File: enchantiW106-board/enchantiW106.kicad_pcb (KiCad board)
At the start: 2 copper layers, 62.2 x 25.4 mm, 66 parts, among them J1 USB_C_Receptacle_USB2.0, SW1 B3U-1000P, SW2 B3U-1000P, U1 USBLC6-2P6, U11 MAX17262REWL+T, U12 BQ25185DLHR, U13 ICM-42670-P, U2 MMC5633NJL, U3 IRIS-W106-00B, U4 NCP167AMX330TBG, U5 CP2102N-Axx-xQFN20, U9 NCP167AMX330TBG

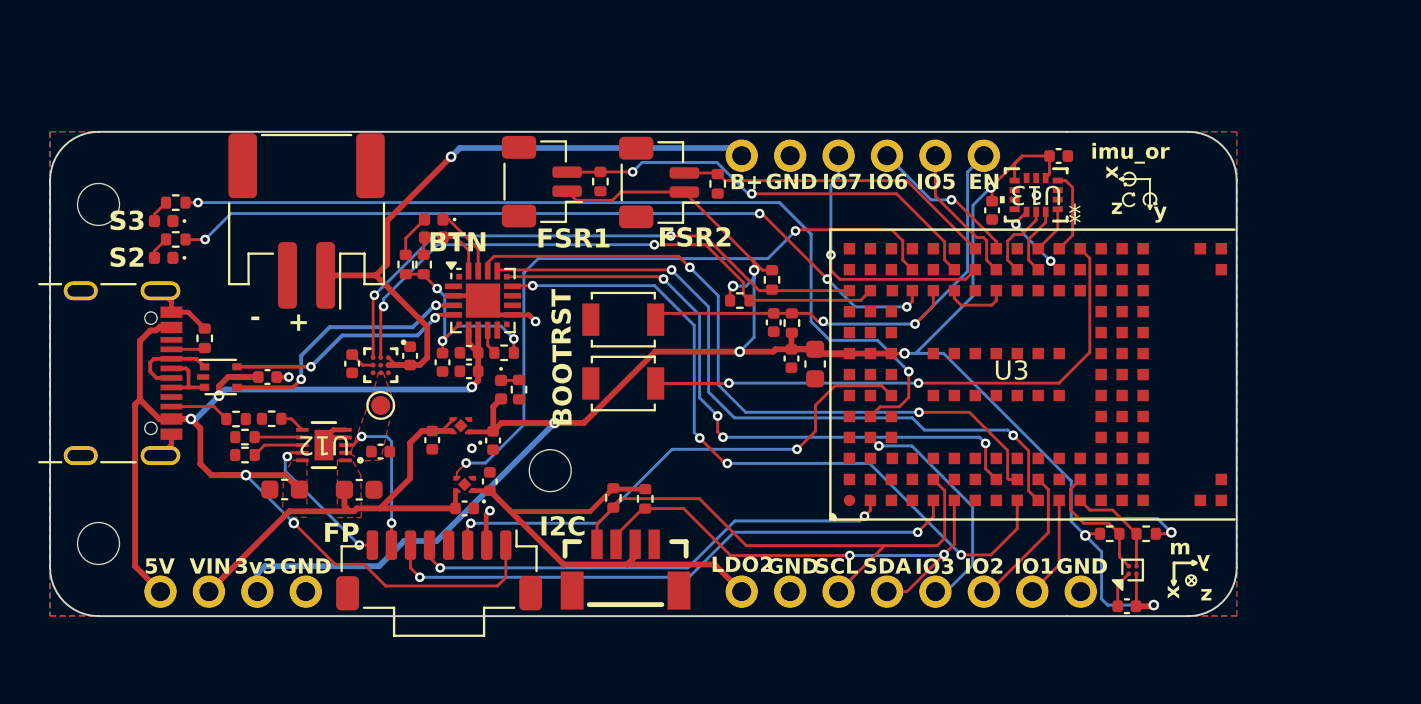
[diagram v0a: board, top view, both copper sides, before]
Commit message: removed all fine pitch components, finished initial board layout and drc check
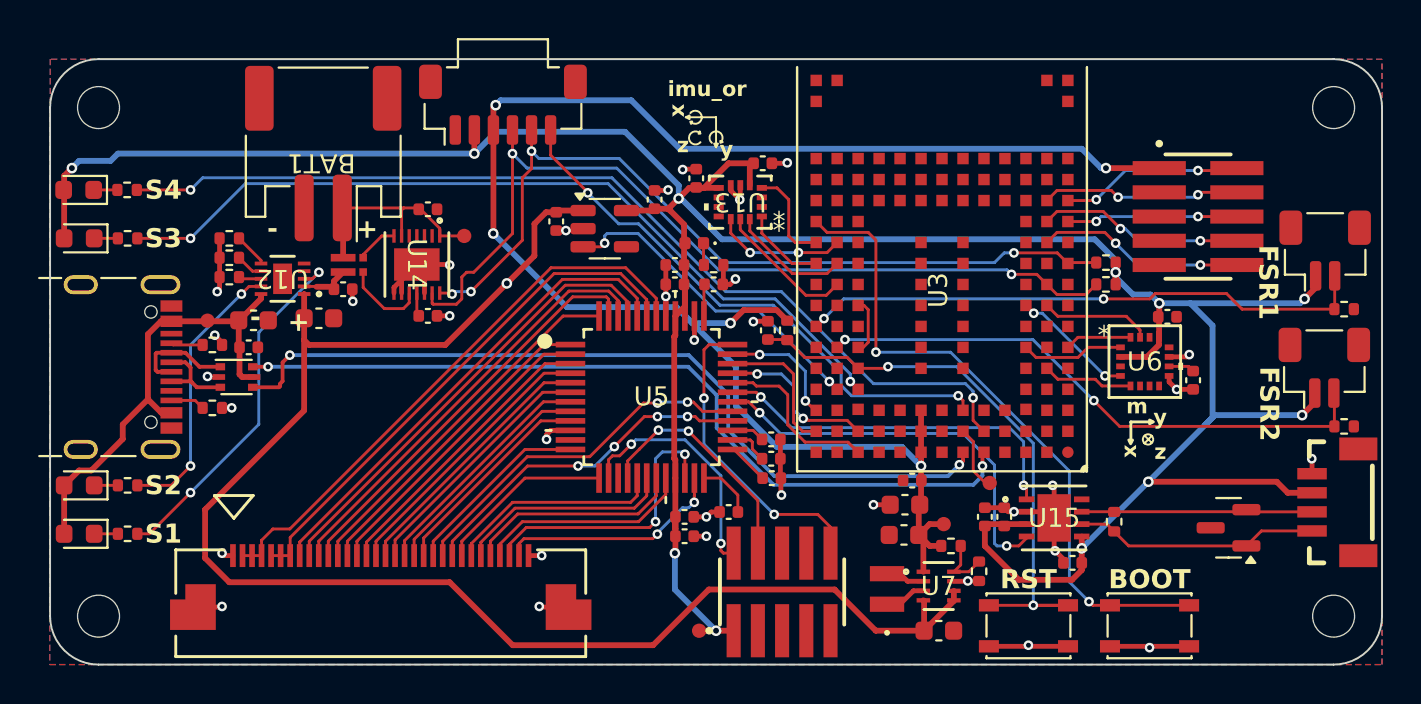
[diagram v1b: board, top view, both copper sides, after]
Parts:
- removed BOARDLAYOUT1: LAYOUT, ENCHANTI_enchanti-board-symbols:enchantiS3-layout
- removed BT1: JST-PH-1x02-2.000mm, Connector_JST:JST_PH_S2B-PH-SM4-TB_1x02-1MP_P2.00mm_Horizontal
- removed C1, C2: 0.1uF, Capacitor_SMD:C_0402_1005Metric
- removed C11, C12: 1uF, Capacitor_SMD:C_0402_1005Metric
- removed C3: 220nF, Capacitor_SMD:C_0402_1005Metric
- removed C8: 0.47uF, Capacitor_SMD:C_0402_1005Metric
- removed FP2: CONN HEADER SMD 6POS 1MM, Connector_Molex:Molex_Pico-Clasp_501331-0807_1x08-1MP_P1.00mm_Vertical
- removed R13: 2k2, Resistor_SMD:R_0402_1005Metric
- removed R14, R16, R18: 1k, Resistor_SMD:R_0402_1005Metric
- removed STATLED1: WIFISTATUS, LED_SMD:LED_0402_1005Metric
- removed STATLED2: GENERAL STATUS, LED_SMD:LED_0402_1005Metric
- removed STATLED3: TX_STAT, LED_SMD:LED_0402_1005Metric
- removed STATLED4: RX_STAT, LED_SMD:LED_0402_1005Metric
- removed TOUCH1: JST-SH-1x04 1.0mm, ENCHANTI_connectors:JST_SMD_1.0mm-4_Vertical
- removed U11: MAX17262REWL+T, ENCHANTI_battery-management:MAX17262
- removed U4, U9: NCP167AMX330TBG, ENCHANTI_regulators:XDFN4_1X1_711AJ_ONS
- added BAT1: JST_SMD_2.0, ENCHANTI_connectors:Battery_JST_2pin, F.Cu at (106.9, 49.4)
- added C10: 1uF, Capacitor_SMD:C_0402_1005Metric, F.Cu at (126.0, 68.5)
- added C14: 0.1uF, Capacitor_SMD:C_0402_1005Metric, F.Cu at (125.5, 55.2)
- added C16: 2.2nF, Capacitor_SMD:C_0402_1005Metric, F.Cu at (128.3, 68.2)
- added C20: 2.2nF, Capacitor_SMD:C_0402_1005Metric, F.Cu at (130.6, 66.4)
- added C24: 2.2nF, Capacitor_SMD:C_0402_1005Metric, F.Cu at (130.5, 65.4)
- added C25: 2.2nF, Capacitor_SMD:C_0402_1005Metric, F.Cu at (130.5, 64.4)
- added C26: 1uF, Capacitor_SMD:C_0402_1005Metric, F.Cu at (125.5, 56.3)
- added C27: 0.1uF, Capacitor_SMD:C_0402_1005Metric, F.Cu at (127.5, 56.3)
- added C28: 1uF, Capacitor_SMD:C_0402_1005Metric, F.Cu at (151.3, 58.0)
- added C29: 10uF, Capacitor_SMD:C_0402_1005Metric, F.Cu at (152.7, 61.3)
- added C30: 47uF, Capacitor_SMD:C_0603_1608Metric, F.Cu at (137.5, 69.4)
- added C31: 0.1uF, Capacitor_SMD:C_0402_1005Metric, F.Cu at (112.5, 52.3)
- added C32: 0.1uF, Capacitor_SMD:C_0402_1005Metric, F.Cu at (146.3, 70.9)
- added C33: 0.1uF, Capacitor_SMD:C_0402_1005Metric, F.Cu at (141.7, 68.5)
- added C34: 1uF, Capacitor_SMD:C_0402_1005Metric, F.Cu at (142.7, 68.5)
- added C46: 0.47uF, Capacitor_SMD:C_0402_1005Metric, F.Cu at (112.5, 57.9)
- added CANFD1: JST-SH-1x04 1.0mm, ENCHANTI_connectors:JST_SMD_1.0mm-4_Vertical, F.Cu at (160.4, 67.7)
- added CHARGLED2: YELLOW_LED, LED_SMD:LED_0603_1608Metric, F.Cu at (94.2, 69.3)
- added D1: NUP2105L, Package_TO_SOT_SMD:SOT-23, F.Cu at (154.5, 69.0)
- added FP1: CONN HEADER SMD 6POS 1MM, Connector_Molex:Molex_Pico-Clasp_501331-0607_1x06-1MP_P1.00mm_Vertical, F.Cu at (116.5, 46.8)
- added H4: MountingHole, MountingHole:MountingHole_2.2mm_M2, F.Cu at (160.0, 47.0)
- added J2: Programming Header, ENCHANTI_connectors:SAMTEC_FTSH-105-01-F-DV-P-TR, F.Cu at (131.1, 72.4)
- added J3: Programming Header, ENCHANTI_connectors:SAMTEC_FTSH-105-01-F-DV-P-TR, F.Cu at (152.9, 52.7)
- added L4: 1uH, ENCHANTI_inductors:CIGT201610, F.Cu at (136.6, 72.2)
- added LED3: USER_LED, LED_SMD:LED_0402_1005Metric, F.Cu at (126.5, 54.1)
- added R29: 120, Resistor_SMD:R_0402_1005Metric, F.Cu at (148.5, 68.7)
- added R38: 2k, Resistor_SMD:R_0402_1005Metric, F.Cu at (96.8, 66.8)
- added R40: 2k, Resistor_SMD:R_0402_1005Metric, F.Cu at (96.8, 69.3)
- added TOUCH2: FFCHEADER, ENCHANTI_connectors:CON_541323262_MOL, F.Cu at (110.0, 73.0)
- added TP2: TestPoint, SparkFun-Connector:TestPoint-0.75mm, F.Cu at (139.6, 68.8)
- added TP4: TestPoint, SparkFun-Connector:TestPoint-0.75mm, F.Cu at (114.4, 53.7)
- added TP6: TestPoint, SparkFun-Connector:TestPoint-0.75mm, F.Cu at (126.7, 74.4)
- added TP7: TestPoint, SparkFun-Connector:TestPoint-0.75mm, F.Cu at (101.0, 58.2)
- added U14: MAX17260SETD+T, ENCHANTI_battery-management:TDFN-14-EP-ADI, F.Cu at (111.9, 55.2)
- added U15: TCAN3413DRBR, ENCHANTI_transceivers:VSON8-DRB_TEX, F.Cu at (145.4, 68.5)
- added U6: MMC5983MA, ENCHANTI_MEMS:MMC5983MA_MEM, F.Cu at (150.1, 60.3)
- added U7: TPS631000DRLR, ENCHANTI_regulators:TPS631000DRLR_TEX, F.Cu at (139.3, 72.1)
- added USER_LED1: BLUE_LED, LED_SMD:LED_0603_1608Metric, F.Cu at (94.2, 53.8)
- added USER_LED3: ORANGE_LED, LED_SMD:LED_0603_1608Metric, F.Cu at (94.2, 51.3)
- C7: value 0.1uF -> 22uF; footprint Capacitor_SMD:C_0402_1005Metric -> Capacitor_SMD:C_0603_1608Metric
- CHARGLED1: value S1 -> RED_LED; footprint LED_SMD:LED_0402_1005Metric -> LED_SMD:LED_0603_1608Metric
- R12: value 2k2 -> 91k
- R4: value 2k2 -> 1mOhm; footprint Resistor_SMD:R_0402_1005Metric -> ENCHANTI_resistors:L4CC0306
- R9: value 2k2 -> 511k
- SW1, SW2: value B3U-1000P -> PTS810; footprint Button_Switch_SMD:SW_SPST_B3U-1000P -> ENCHANTI_switches:SW_SPST_PTS810
- TP1: footprint TestPoint:TestPoint_Pad_D1.0mm -> SparkFun-Connector:TestPoint-0.75mm
- U2: value MMC5633NJL -> TPS7A2033PDBVR; footprint Package_BGA:WLP-4_0.86x0.86mm_P0.4mm -> Package_TO_SOT_SMD:SOT-23-5
- U5: value CP2102N-Axx-xQFN20 -> CY8C4149AZI-S593; footprint Package_DFN_QFN:SiliconLabs_QFN-20-1EP_3x3mm_P0.5mm_EP1.8x1.8mm -> ENCHANTI_mcus:TQFP48_INFINEON
- moved R4 42.3 mm to (108.4, 55.2), turned to -90 degrees
- moved H3 41.8 mm to (160.0, 73.7)
- moved ANG1 41.2 mm to (159.6, 54.5), turned to 0 degrees
- moved R1 39.6 mm to (160.6, 57.6), turned to 180 degrees
- moved ANG3 36.2 mm to (159.5, 60.6), turned to 0 degrees
- moved R2 35.2 mm to (160.6, 63.7), turned to 180 degrees
- moved U2 33.0 mm to (121.8, 53.3), turned to 0 degrees
- moved TP1 32.2 mm to (142.0, 66.7)
- moved SW2 31.9 mm to (150.4, 74.2), turned to 0 degrees
- moved C7 31.3 mm to (139.3, 74.4), turned to 0 degrees
- moved SW1 24.8 mm to (144.0, 74.2), turned to 0 degrees
- moved CHARGLED1 22.7 mm to (94.2, 66.8), turned to 180 degrees
- moved R19 19.3 mm to (148.1, 55.1), turned to 0 degrees
- moved R12 17.9 mm to (141.4, 71.3)
- moved R20 17.5 mm to (148.1, 56.3), turned to 0 degrees
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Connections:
- ANG1 pad 1: +3V3 -> 3V3_AUX
- ANG3 pad 1: +3V3 -> 3V3_AUX
- C17 pad 1: +3V3 -> 3V3_AUX
- C18 pad 1: +3V3 -> 3V3_AUX
- C6 pad 1: VUSB -> GND
- C6 pad 2: GND -> 3V3_AUX
- C7 pad 1: +BATT -> SYS
- CHARGLED1 pad 2: +3V3 -> VUSB
- R10 pad 1: /ORANGELED -> Net-(USER_LED3-K)
- R10 pad 2: Net-(STATLED2-A) -> /ORANGELED
- R12 pad 1: /SDA3 -> GND
- R12 pad 2: 3V3_AUX -> Net-(U7-FB)
- R19 pad 2: +3V3 -> 3V3_AUX
- R20 pad 2: +3V3 -> 3V3_AUX
- R3 pad 1: Net-(CHARGLED1-K) -> Net-(LED3-K)
- R4 pad 1: /SCL2 -> +BATT
- R4 pad 2: +3V3 -> CHRG+
- R8 pad 1: /BLUELED -> Net-(USER_LED1-K)
- R8 pad 2: Net-(STATLED1-A) -> /BLUELED
- R9 pad 1: /SDA2 -> Net-(U7-FB)
- SW1 pad 1: /BOOT -> /EN
- SW2 pad 1: /EN -> /BOOT
- TP1 pad 1: CHRG+ -> /USB_ID
- U13 pad 5: +3V3 -> 3V3_AUX
- U13 pad 8: +3V3 -> 3V3_AUX
- U3 pad A10: /TXD -> /SCL
- U3 pad A11: /IO11 -> unconnected-(U3A-GPIO[11]DTR-PadA11)
- U3 pad A12: /SDA2 -> /JTAG_TDO
- U3 pad A14: unconnected-(U3A-JTAG_TMS-PadA14) -> /JTAG_TMS
- U3 pad A5: /LED2 -> unconnected-(U3A-QSPI_RCE-PadA5)
- U3 pad A6: /SDA3 -> /MAG_COPI
- U3 pad A9: /CTS -> unconnected-(U3A-SDIO_D1-PadA9)
- U3 pad B10: /IO12 -> unconnected-(U3A-GPIO[12]DSR-PadB10)
- U3 pad B11: unconnected-(U3A-JTAG_nRST-PadB11) -> /JTAG_nRST
- U3 pad B12: /SCL2 -> /JTAG_TDI
- U3 pad B14: unconnected-(U3A-JTAG_TCK-PadB14) -> /JTAG_TCK
- U3 pad B5: /SCL3 -> /MAG_CIPO
- U3 pad B8: /RTS -> /MAG_INT
- U3 pad B9: /RXD -> /SDA
- U3 pad C6: unconnected-(U3A-SDIO_CLK-PadC6) -> /MAG_SCLK
- U3 pad C8: unconnected-(U3A-SDIO_D3-PadC8) -> /MAG_CS
- U3 pad E1: unconnected-(U3A-USB_DM-PadE1) -> /USBD-
- U3 pad F1: unconnected-(U3A-USB_DP-PadF1) -> /USBD+
- U3 pad F2: unconnected-(U3A-USB_ID-PadF2) -> /USB_ID
- U3 pad F3: /BTN -> /BUTTON_FP
- U3 pad L1: /SDA -> /TOUCH_COPI
- U3 pad L2: /SCL -> /TOUCH_CIPO
- U3 pad M6: /FSR1 -> /FSR2
- U3 pad M7: /IO44 -> unconnected-(U3A-GPIO[44]-PadM7)
- U3 pad M8: /IO42 -> unconnected-(U3A-GPIO[42]-PadM8)
- U3 pad N2: unconnected-(U3A-GPIO[54]-PadN2) -> /TOUCH_SCLK
- U3 pad N3: unconnected-(U3A-GPIO[53]-PadN3) -> /TOUCH_CS
- U3 pad N7: /FSR2 -> /FSR1
- U3 pad N8: /IO43 -> unconnected-(U3A-GPIO[43]-PadN8)
- U5 pad 1: unconnected-(U5-RS485/GPIO.1-Pad1) -> /MSC007
- U5 pad 10: unconnected-(U5-NC-Pad10) -> GND
- U5 pad 12: GND -> /MSC030
- U5 pad 13: unconnected-(U5-~{WAKEUP}-Pad13) -> /MSC031
- U5 pad 14: unconnected-(U5-SUSPEND-Pad14) -> /SWDA
- U5 pad 15: /CTS -> unconnected-(U5-NC_2-Pad15)
- U5 pad 16: /RTS -> /SWCLK
- U5 pad 17: /TXD -> /MSC034
- U5 pad 18: /RXD -> /MSC035
- U5 pad 19: Net-(STATLED4-K) -> /MSC036
- U5 pad 2: unconnected-(U5-CLK/GPIO.0-Pad2) -> /MSC008
- U5 pad 20: Net-(STATLED3-K) -> /MSC037
- U5 pad 21: GND -> 3V3_AUX
- U5 pad 3: GND -> /MSC009
- U5 pad 4: /USBD+ -> /MSC010
- U5 pad 5: /USBD- -> /MSC011
- U5 pad 6: VDD -> /MSC012
- U5 pad 7: VUSB -> /MSC013
- U5 pad 8: VUSB -> /MSC014
- U5 pad 9: /RST -> /MSC015
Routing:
- net 3V3_AUX: track 25.1 -> 163.8 mm, vias 0 -> 11
- net SYS: track 24.4 -> 80.7 mm, vias 0 -> 1
- net VUSB: track 69.2 -> 24.7 mm, vias 5 -> 0
- net GND: track 17.2 -> 58.0 mm, vias 5 -> 34
- net /CTS: track 37.7 -> 0.00 mm, vias 4 -> 0
- net /TXD: track 37.2 -> 0.00 mm, vias 2 -> 0
- net /RXD: track 36.8 -> 0.00 mm, vias 2 -> 0
- net /RTS: track 33.9 -> 0.00 mm, vias 4 -> 0
- net /LED2: track 31.0 -> 0.00 mm, vias 2 -> 0
- net /USBD-: track 12.5 -> 43.3 mm
- net /MSC000: track 0.00 -> 30.0 mm
- net /USBD+: track 13.9 -> 43.1 mm
- net +3V3: track 119.3 -> 90.1 mm, vias 9 -> 5
- net /BUTTON_FP: track 0.00 -> 29.2 mm, vias 0 -> 2
- net /SCL3: track 27.8 -> 0.00 mm
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- removed copper zone on F.Cu, net CHRG+
- removed copper zone on F.Cu, net SYS
- removed copper zone on F.Cu, net VUSB
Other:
- board size 62.2 x 25.4 mm -> 69.9 x 31.8 mm
- board text added: "EnchantiW106 v0.4 2025-06 Albert Niyonsenga"
- board text added: "S1"
- board text added: "S4"
- board text removed: "2 pin JST-PH Vertical Header"
- board text removed: "2 pin JST-SH Vertical Header"
- board text removed: "3v3"
- board text removed: "4 pin JST-SH Vertical Header"
- board text removed: "B+"
- board text removed: "BTN"
- board text removed: "Boot Button"
- board text removed: "EN"
- board text removed: "ESP32-S3 WROOM 2"
- board text removed: "EnchantiW106 v0.1 2024-10 Albert Niyonsenga"
- board text removed: "FP"
- board text removed: "Fuel Gauge"
- board text removed: "GND"
- board text removed: "I2C"
- board text removed: "ICM20948"
- board text removed: "IO1"
- board text removed: "IO2"
- board text removed: "IO3"
- board text removed: "IO5"
- board text removed: "IO6"
- board text removed: "IO7"
- board text removed: "Indicator LEDs (RED)"
- board text removed: "LDO2"
- board text removed: "MCP73871"
- board text removed: "NCP167AMX 180TBG"
- board text removed: "NCP167AMX 330TBG"
- board text removed: "Neopixel"
- board text removed: "Ohmite LVK12 Shunt Resistor"
- board text removed: "Reset Button"
- board text removed: "SCL"
- board text removed: "SDA"
- board text removed: "USB C Receptacle"
- board text removed: "USBLC6-LP6"
- board text removed: "VIN"

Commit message: update gitignore, to ignore schematic/pcb lock files, fixed DRC errors and warnings
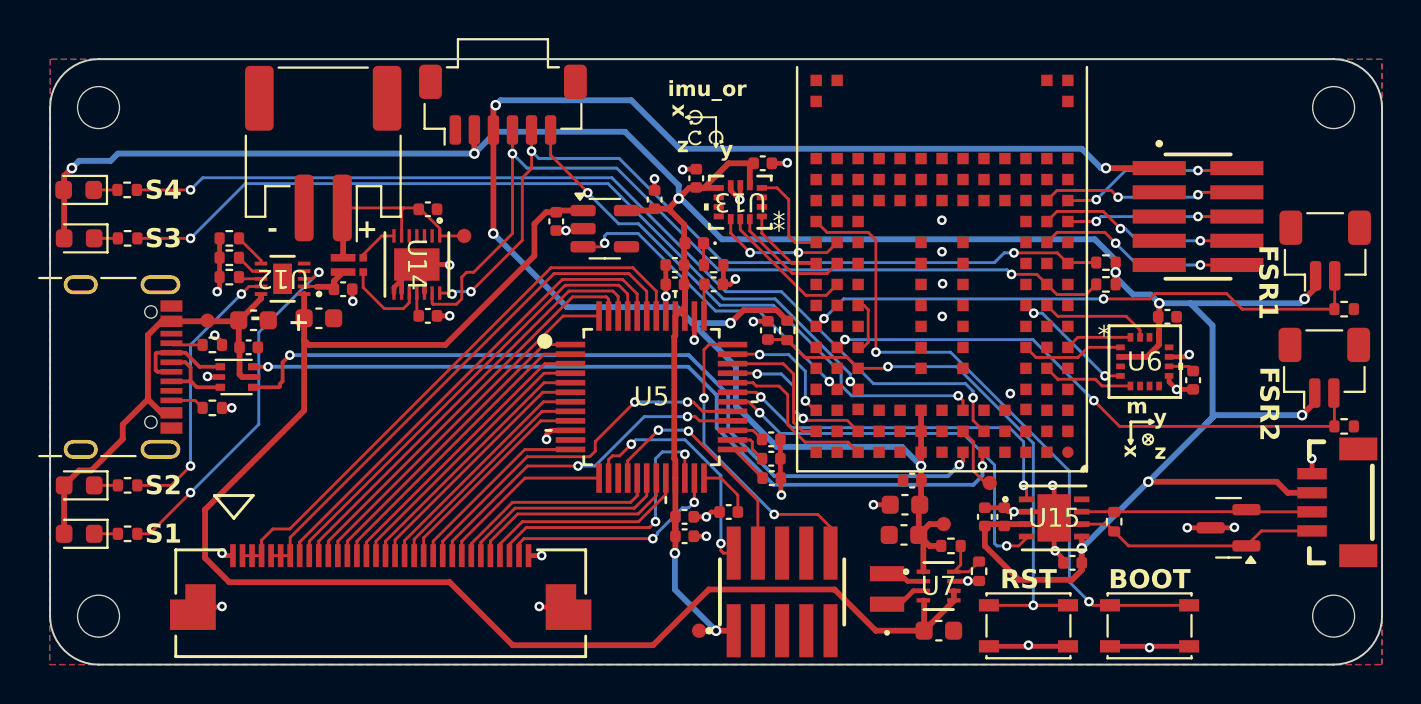
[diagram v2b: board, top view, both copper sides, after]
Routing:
- net GND: track 58.0 -> 60.4 mm, vias 34 -> 41
- net /MSC114: vias 4 -> 2
- net SYS: vias 1 -> 0
